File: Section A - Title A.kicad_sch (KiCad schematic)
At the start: 0 parts

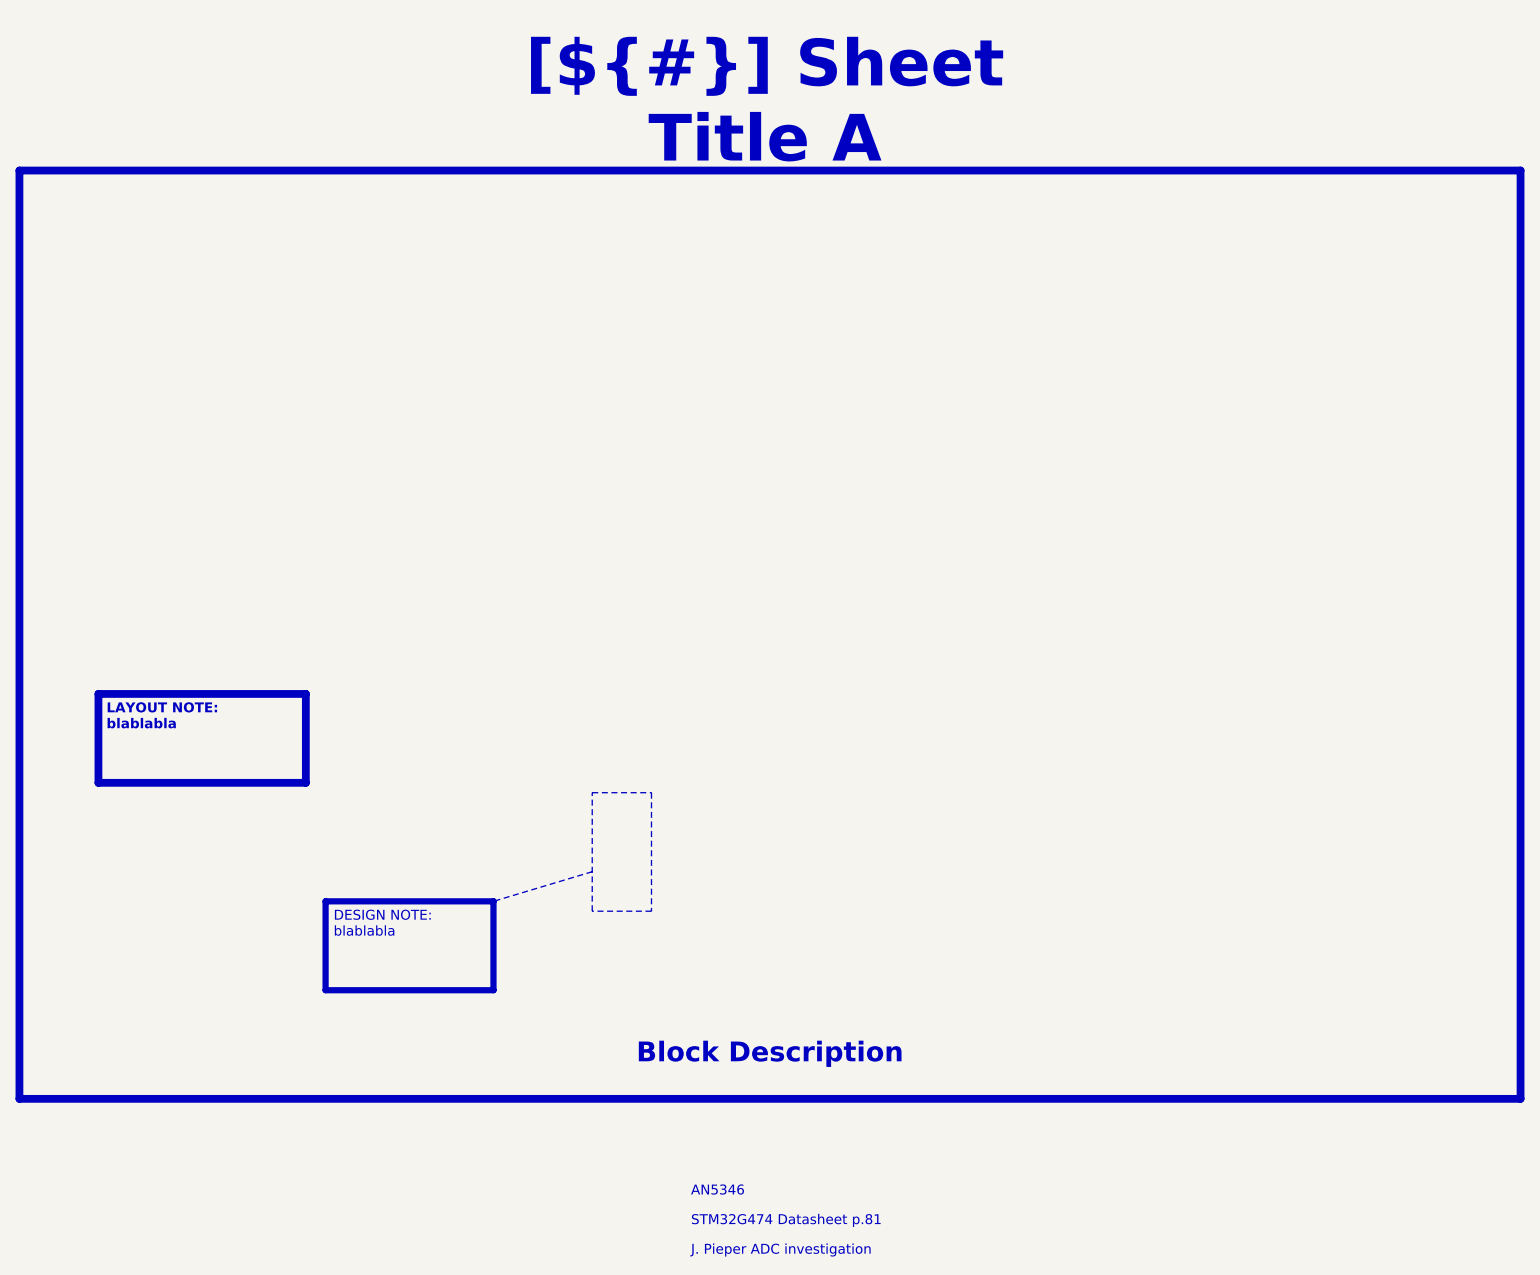
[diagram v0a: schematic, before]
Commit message: feat: Changed templates to be specific to Ryan Dynamics
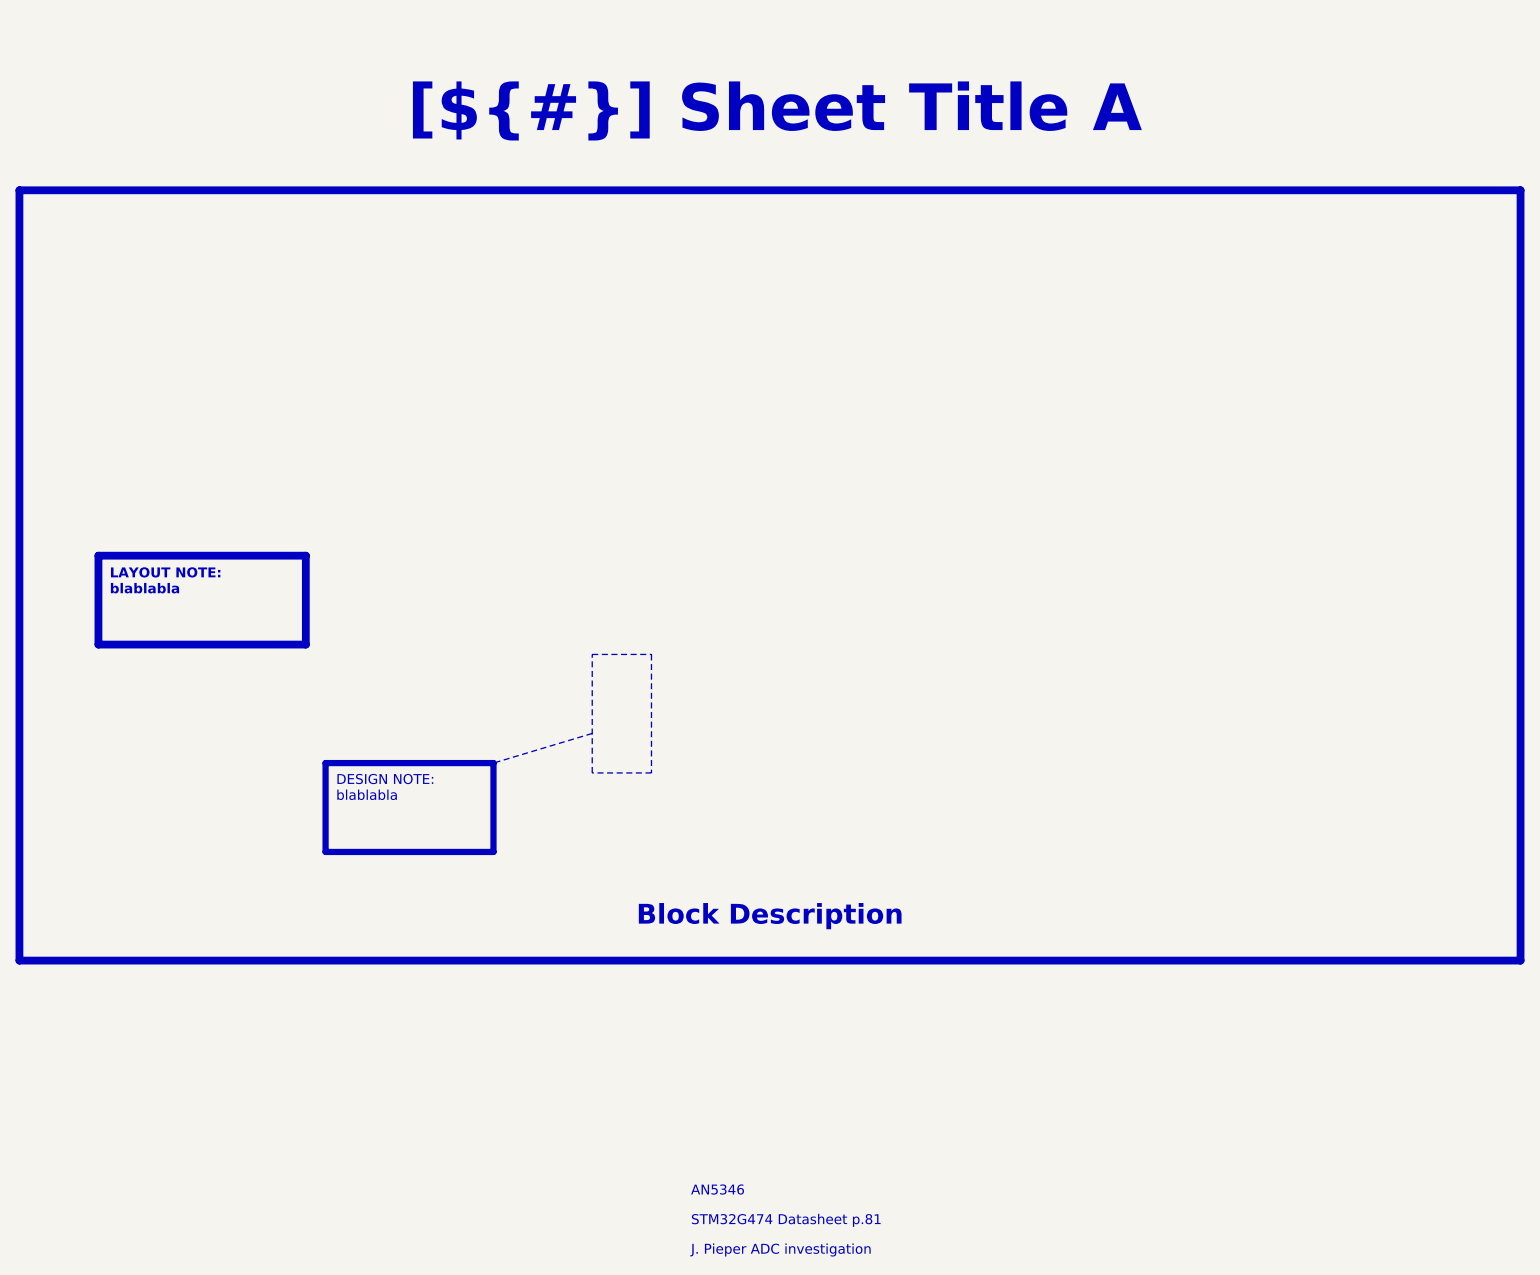
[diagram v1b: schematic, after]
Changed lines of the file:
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@@
 (kicad_sch
-	(version 20231120)
+	(version 20250114)
 	(generator "eeschema")
-	(generator_version "8.0")
+	(generator_version "9.0")
 	(paper "A4")
 	(title_block
@@
 		(company "${COMPANY}")
 	)
-	(polyline
-		(pts
-			(xy 129.54 120.65) (xy 116.84 124.46)
-		)
-		(stroke
-			(width 0)
-			(type dot)
-			(color 255 0 0 1)
-		)
-	)
 	(rectangle
-		(start 129.54 110.49)
-		(end 137.16 125.73)
+		(start 129.54 92.71)
+		(end 137.16 107.95)
 		(stroke
 			(width 0)
@@
 	)
 	(rectangle
-		(start 55.88 30.48)
-		(end 248.92 149.86)
+		(start 55.88 33.02)
+		(end 248.92 132.08)
 		(stroke
 			(width 1)
@@
 		(fill
 			(type none)
-		)
-	)
-	(text_box "LAYOUT NOTE:\nblablabla"
-		(exclude_from_sim no)
-		(at 66.04 97.79 0)
-		(size 26.67 11.43)
-		(stroke
-			(width 1)
-			(type solid)
-			(color 0 0 255 1)
-		)
-		(fill
-			(type none)
-		)
-		(effects
-			(font
-				(face "Arial")
-				(size 1.27 1.27)
-				(thickness 0.4)
-				(bold yes)
-				(color 0 0 255 1)
-			)
-			(justify left top)
-		)
-	)
-	(text_box "[${#}] ${TITLE}"
-		(exclude_from_sim no)
-		(at 115.57 15.24 0)
-		(size 72.39 12.7)
-		(stroke
-			(width -0.0001)
-			(type default)
-		)
-		(fill
-			(type none)
-		)
-		(effects
-			(font
-				(face "Times New Roman")
-				(size 6 6)
-				(thickness 1.2)
-				(bold yes)
-				(color 162 22 34 1)
-			)
-		)
-	)
-	(text_box "Block Description"
-		(exclude_from_sim no)
-		(at 57.15 139.7 0)
-		(size 190.5 7.62)
-		(stroke
-			(width -0.0001)
-			(type default)
-		)
-		(fill
-			(type none)
-		)
-		(effects
-			(font
-				(face "Times New Roman")
-				(size 2.54 2.54)
-				(thickness 0.508)
-				(bold yes)
-				(color 162 22 34 1)
-			)
-			(justify bottom)
-		)
-	)
-	(text_box "DESIGN NOTE:\nblablabla"
-		(exclude_from_sim no)
-		(at 95.25 124.46 0)
-		(size 21.59 11.43)
-		(stroke
-			(width 0.8)
-			(type solid)
-			(color 250 236 0 1)
-		)
-		(fill
-			(type none)
-		)
-		(effects
-			(font
-				(face "Arial")
-				(size 1.27 1.27)
-				(color 0 0 0 1)
-			)
-			(justify left top)
 		)
 	)
@@
 		)
 	)
+	(text_box "LAYOUT NOTE:\nblablabla"
+		(exclude_from_sim no)
+		(at 66.04 80.01 0)
+		(size 26.67 11.43)
+		(margins 1.4525 1.4525 1.4525 1.4525)
+		(stroke
+			(width 1)
+			(type solid)
+			(color 0 0 255 1)
+		)
+		(fill
+			(type none)
+		)
+		(effects
+			(font
+				(face "Arial")
+				(size 1.27 1.27)
+				(thickness 0.4)
+				(bold yes)
+				(color 0 0 255 1)
+			)
+			(justify left top)
+		)
+	)
+	(text_box "[${#}] ${TITLE}"
+		(exclude_from_sim no)
+		(at 99.06 15 0)
+		(size 107.9128 15)
+		(margins 4.4999 4.4999 4.4999 4.4999)
+		(stroke
+			(width -0.0001)
+			(type default)
+		)
+		(fill
+			(type none)
+		)
+		(effects
+			(font
+				(size 6 6)
+				(thickness 1.2)
+				(bold yes)
+				(color 162 22 34 1)
+			)
+		)
+	)
+	(text_box "Block Description"
+		(exclude_from_sim no)
+		(at 57.15 121.92 0)
+		(size 190.5 7.62)
+		(margins 1.9049 1.9049 1.9049 1.9049)
+		(stroke
+			(width -0.0001)
+			(type default)
+		)
+		(fill
+			(type none)
+		)
+		(effects
+			(font
+				(size 2.54 2.54)
+				(thickness 0.508)
+				(bold yes)
+				(color 162 22 34 1)
+			)
+			(justify bottom)
+		)
+	)
+	(text_box "DESIGN NOTE:\nblablabla"
+		(exclude_from_sim no)
+		(at 95.25 106.68 0)
+		(size 21.59 11.43)
+		(margins 1.3525 1.3525 1.3525 1.3525)
+		(stroke
+			(width 0.8)
+			(type solid)
+			(color 250 236 0 1)
+		)
+		(fill
+			(type none)
+		)
+		(effects
+			(font
+				(face "Arial")
+				(size 1.27 1.27)
+				(color 0 0 0 1)
+			)
+			(justify left top)
+		)
+	)
+	(polyline
+		(pts
+			(xy 129.54 102.87) (xy 116.84 106.68)
+		)
+		(stroke
+			(width 0)
+			(type dot)
+			(color 255 0 0 1)
+		)
+	)
